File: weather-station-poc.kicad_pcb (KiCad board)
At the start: 4 copper layers, 155 x 88 mm, 136 parts, among them IC1 632723100011, IC2 TCPP01-M12, IC3 USBLC6-2SC6, IC4 BME690, IC5 S2-LPQTR, IC6 BALF-SPI2-01D3, IC7 STSAFA110S8OCD03, J1 Conn_ARM_JTAG_SWD_10, J2 61300311121, J3 61300311121, J4 61300511121, J5 61300311121, J6 687140149022, J7 687110149022, Q1 STL11N3LLH6, U1 STM32U5G9ZJTxQ, U2 BME280, U3 BMP581, Y1 NX2016SA-16MHZ-EXS00A-CS07826, Y2 NX2012SA-32.768K-STD-MUB-1, Y3 NX1612SA-50M-EXS00A-CS08403

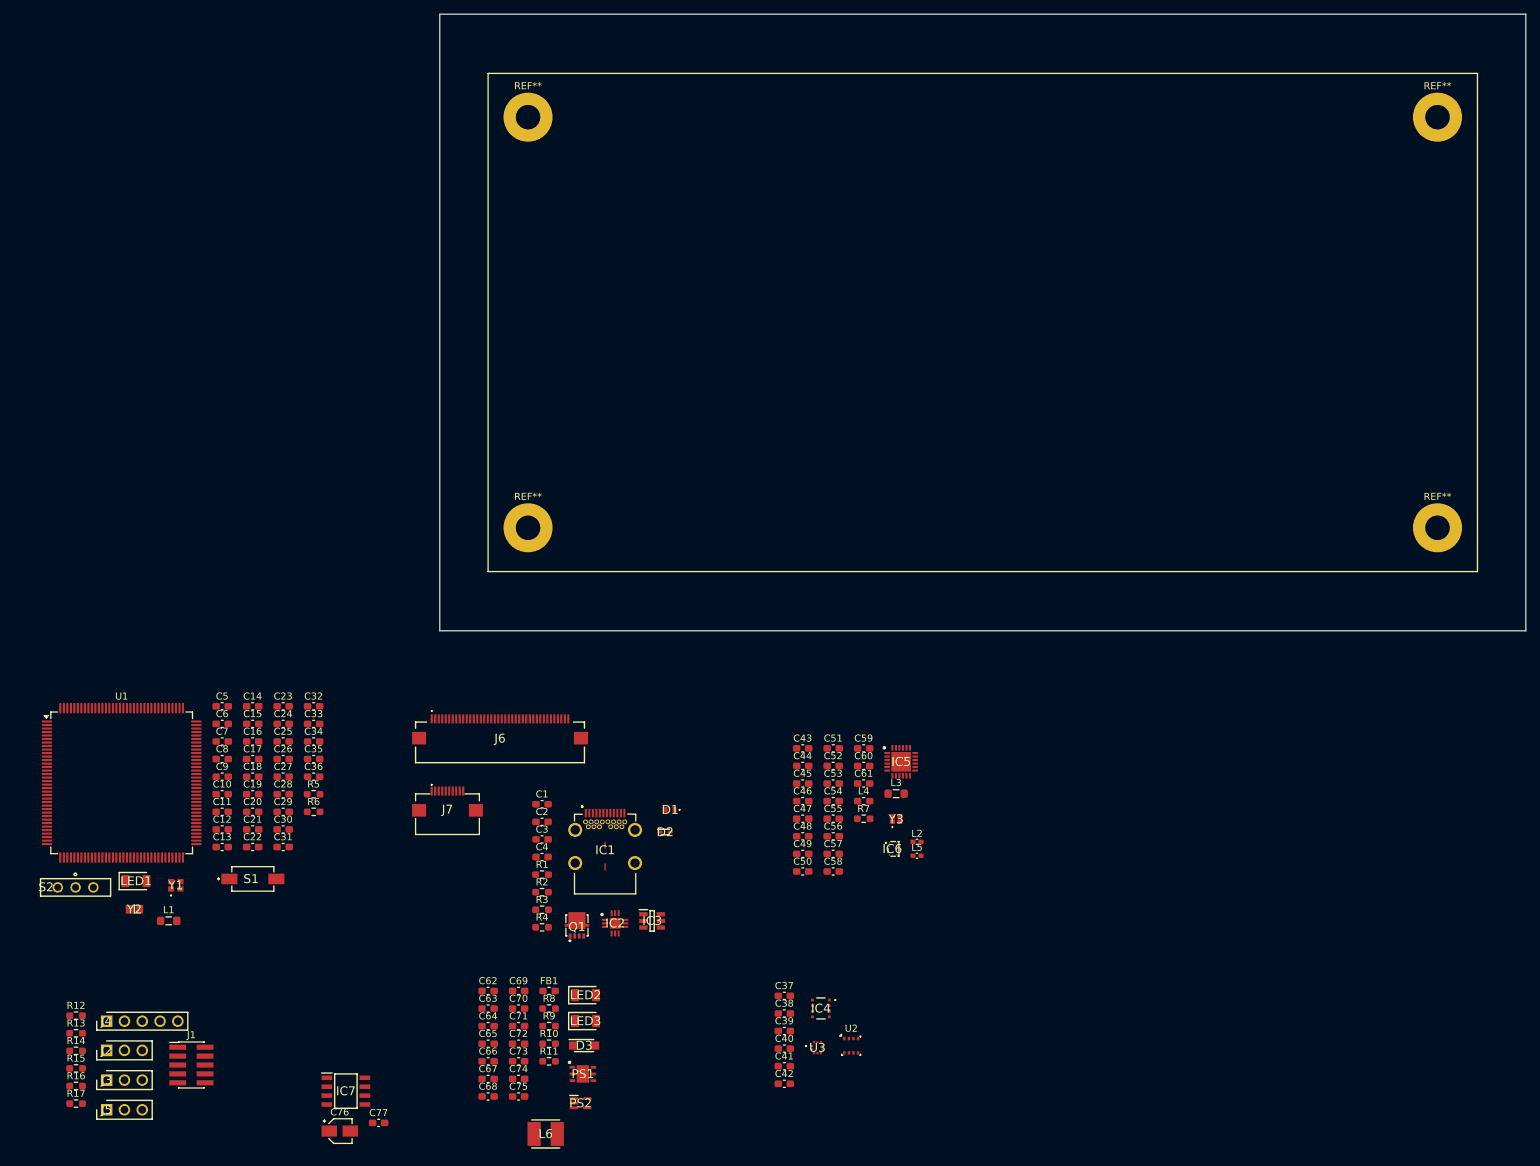
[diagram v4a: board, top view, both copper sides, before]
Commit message: LCD 10 pins connector is top and not bottom face, replace connector part
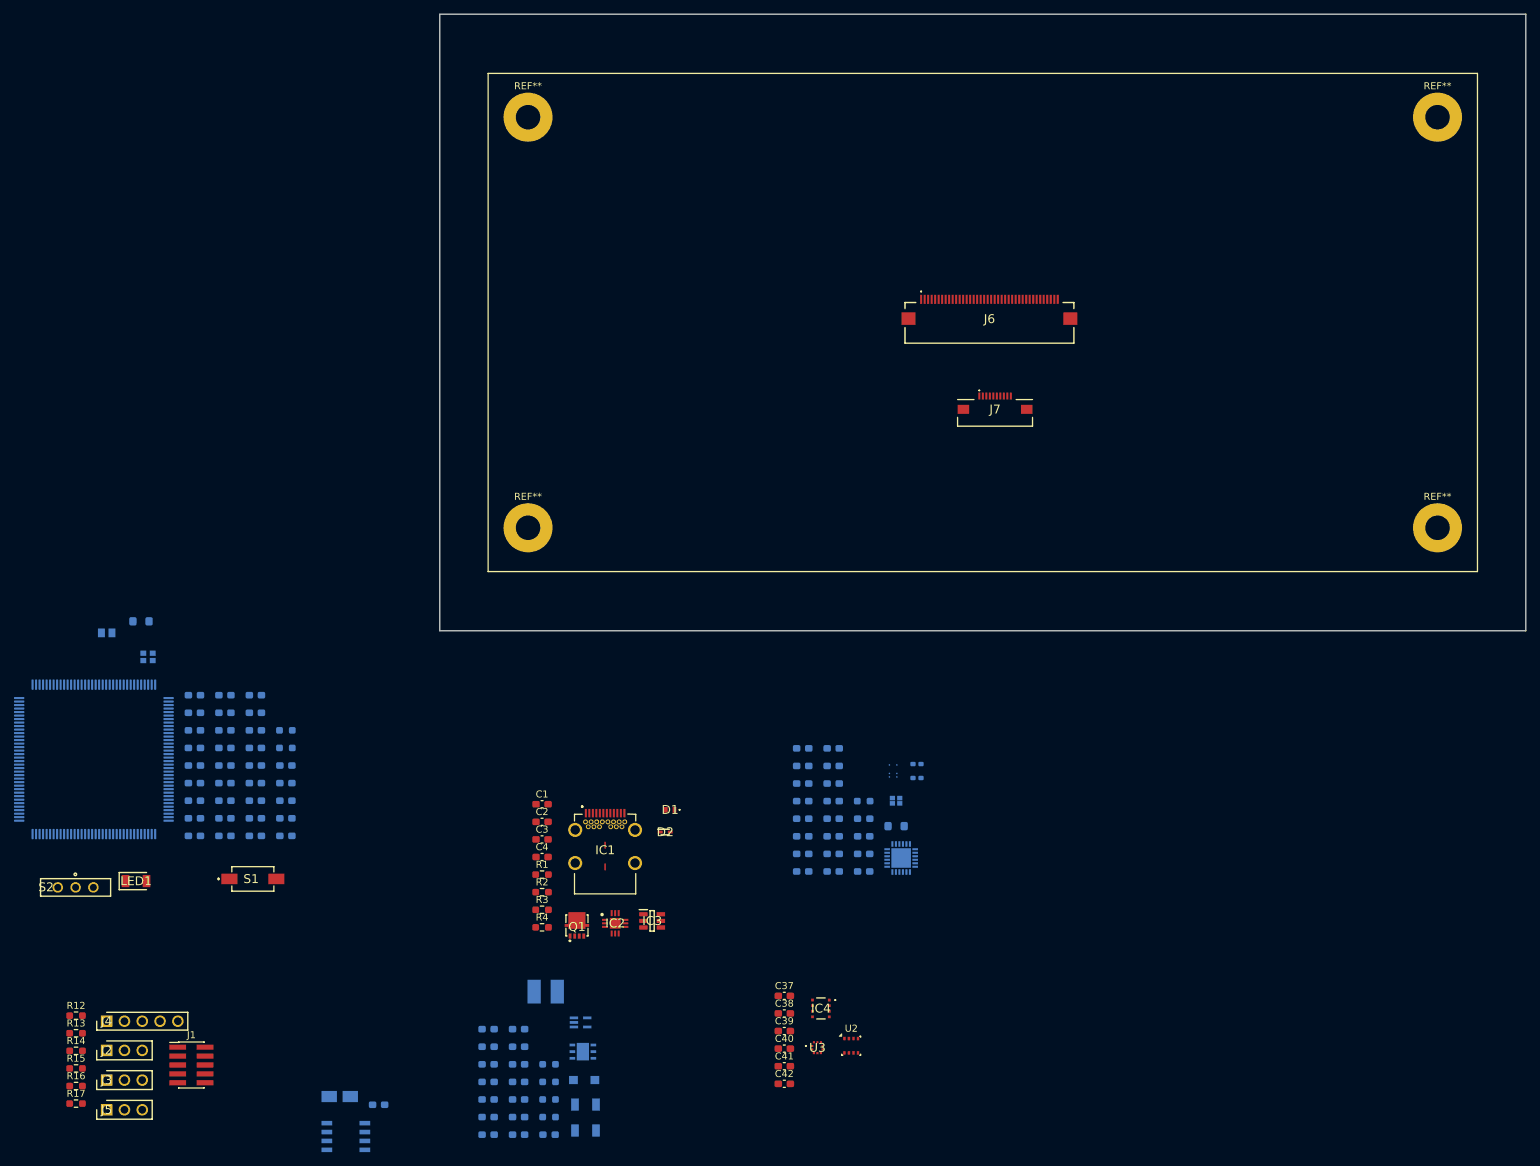
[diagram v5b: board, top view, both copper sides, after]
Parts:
- C10, C11, C12, C13, C14, C15, C16, C17, C18, C19, C20, C21, C22, C23, C24, C25, C26, C27, C28, C29, C30, C31, C32, C33, C34, C35, C36, C43, C44, C45, C46, C47, C48, C49, C5, C50, C51, C52, C53, C54, C55, C56, C57, C58, C59, C6, C60, C61, C62, C63, C64, C65, C66, C67, C68, C69, C7, C70, C71, C72, C73, C74, C75, C76, C77, C8, C9, D3, FB1, IC5, IC6, IC7, L1, L2, L3, L4, L5, L6, LED2, LED3, PS1, PS2, R10, R11, R5, R6, R7, R8, R9, U1, Y1, Y2, Y3: moved to B.Cu
- J7: value 687110149022 -> 687110183622; footprint weather-station-poc-fp:687110149022 -> weather-station-poc-fp:687110183622
- moved J7 95.5 mm to (164.7, 88.7)
- moved J6 92.0 mm to (163.8, 76.1)
- moved L1 42.9 mm to (42.8, 119.0)
- moved Y2 39.6 mm to (37.9, 120.6)
- moved Y1 32.8 mm to (43.8, 124.0)
- moved C13 22.0 mm to (50.4, 129.5)
- moved C22 22.0 mm to (54.7, 129.5)
- moved C31 22.0 mm to (59.1, 129.5)
- moved C62 20.5 mm to (92.3, 192.2)
- moved C69 20.5 mm to (96.7, 192.2)
- moved FB1 20.5 mm to (101.0, 192.2)
- moved L6 20.3 mm to (100.5, 171.8)
- moved LED2 19.3 mm to (106.2, 191.6)
- moved C14 18.9 mm to (54.7, 149.6)
- moved C32 18.9 mm to (63.4, 149.6)
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
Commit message: Place MCU and its components around
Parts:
- removed the C29 at (59.1, 134.5)
- moved S2 207.4 mm to (232.1, 89.0), turned to 180 degrees
- moved C31 144.6 mm to (177.7, 61.0), turned to -90 degrees
- moved U1 141.4 mm to (162.9, 76.3)
- moved L1 140.6 mm to (170.4, 60.2), turned to 180 degrees
- moved C9 140.4 mm to (168.1, 62.9), turned to 90 degrees
- moved C23 138.6 mm to (176.3, 75.6)
- moved C8 138.2 mm to (176.3, 85.0)
- moved C10 137.4 mm to (166.1, 62.9), turned to 90 degrees
- moved C28 137.1 mm to (173.2, 61.0), turned to -90 degrees
- moved C24 135.7 mm to (176.3, 78.6)
- moved C29 135.7 mm to (174.7, 61.0), turned to -90 degrees
- moved C30 135.7 mm to (176.2, 61.0), turned to -90 degrees
- moved C21 134.5 mm to (170.2, 62.9), turned to 90 degrees
- moved C22 134.2 mm to (176.3, 72.6)
- moved C20 129.9 mm to (163.2, 62.9), turned to 90 degrees
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- renumbered C30 to C29, C31 to C30, C32 to C31, C33 to C32, C34 to C33, C35 to C34, C36 to C35, C37 to C36, C38 to C37, C39 to C38, C40 to C39, C41 to C40, C42 to C41, C43 to C42, C44 to C43, C45 to C44, C46 to C45, C47 to C46, C48 to C47, C49 to C48, C50 to C49, C51 to C50, C52 to C51, C53 to C52, C54 to C53, C55 to C54, C56 to C55, C57 to C56, C58 to C57, C59 to C58, C60 to C59, C61 to C60, C62 to C61, C63 to C62, C64 to C63, C65 to C64, C66 to C65, C67 to C66, C68 to C67, C69 to C68, C70 to C69, C71 to C70, C72 to C71, C73 to C72, C74 to C73, C75 to C74, C76 to C75, C77 to C76
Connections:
- C28 pad 1: +3V3_CONT -> /MCU/VDD11

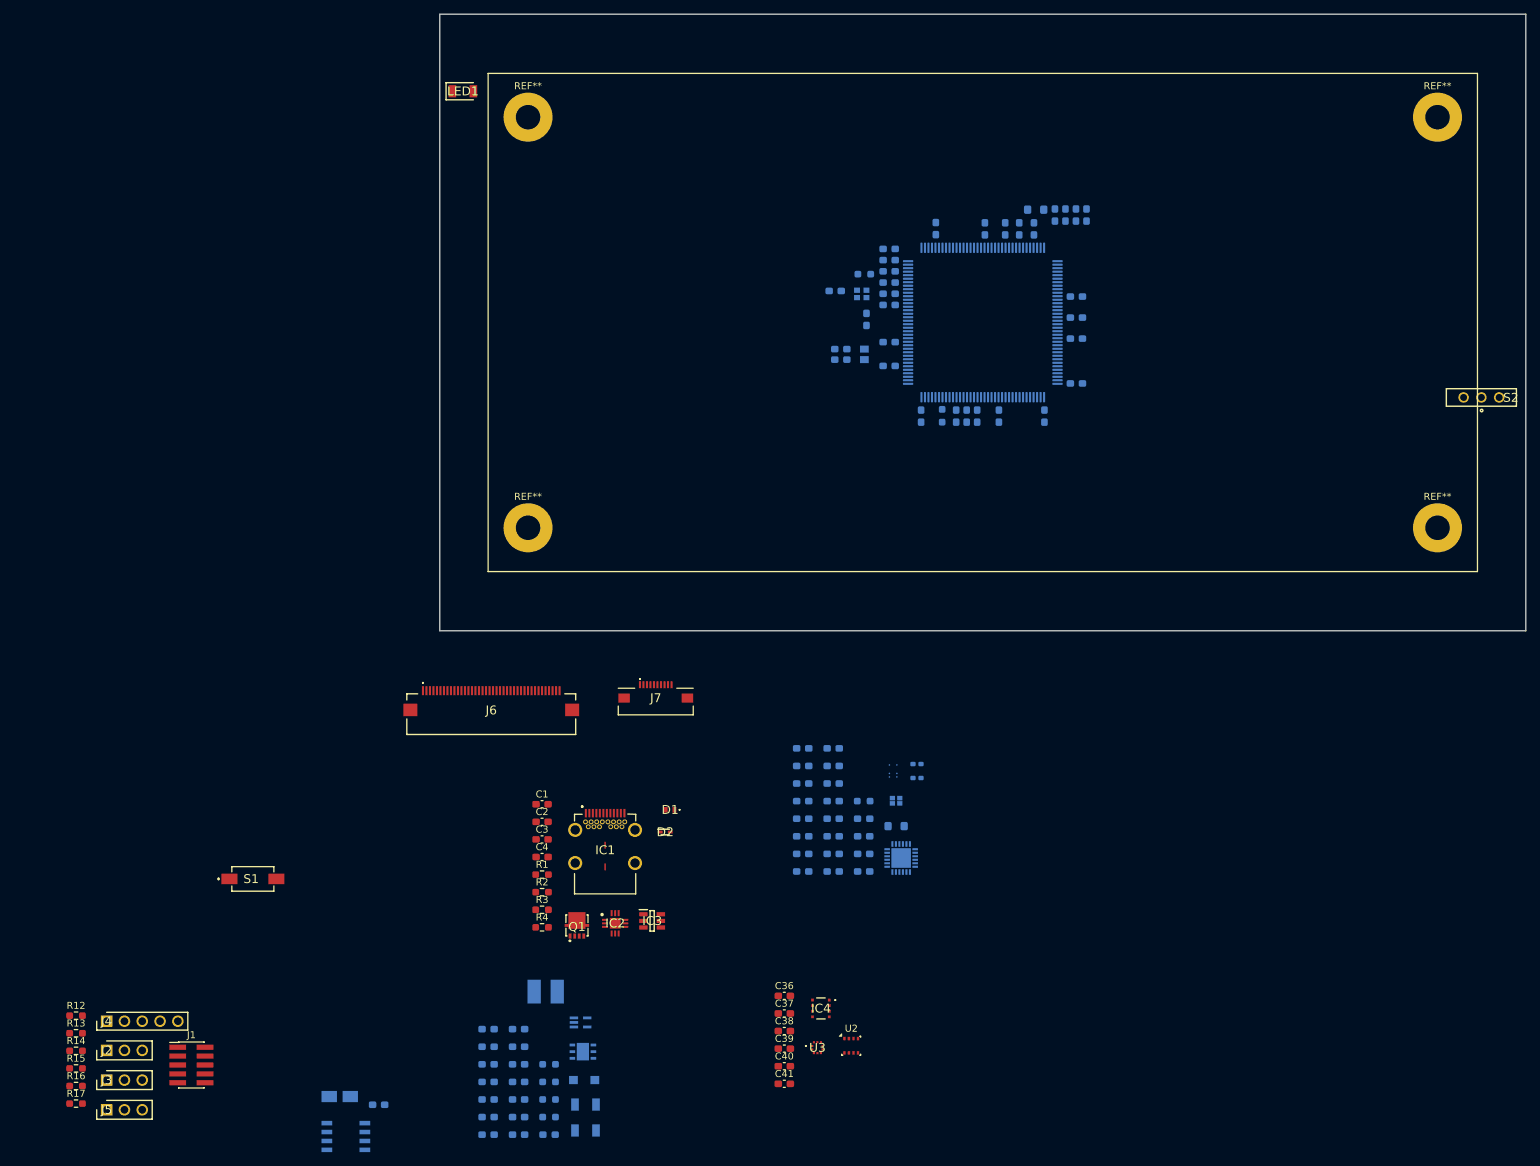
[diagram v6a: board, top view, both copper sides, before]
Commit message: Place power supplies components and STSAFE
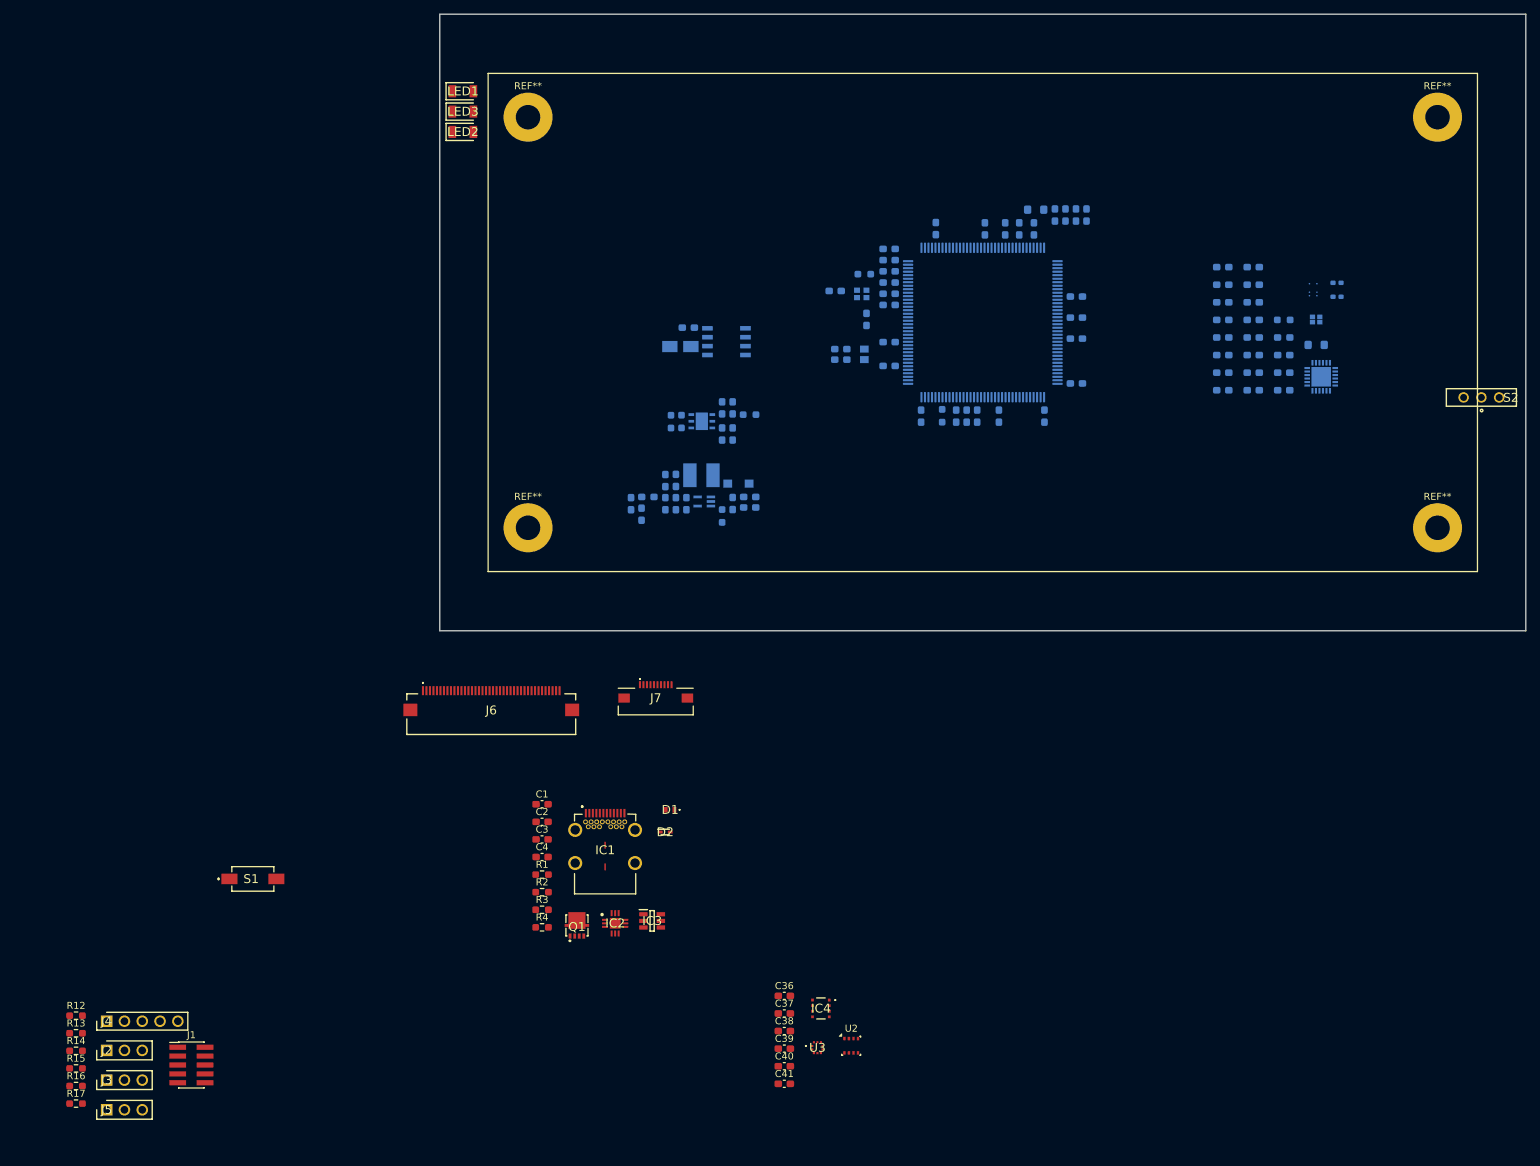
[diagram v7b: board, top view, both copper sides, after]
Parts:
- LED2, LED3: moved to F.Cu
- moved LED2 143.6 mm to (88.7, 49.1)
- moved LED3 142.8 mm to (88.7, 46.2)
- moved IC7 125.8 mm to (126.3, 79.0)
- moved C76 119.4 mm to (120.9, 77.0), turned to 180 degrees
- moved C75 117.6 mm to (119.7, 79.7), turned to 180 degrees
- moved C61 105.9 mm to (127.2, 92.2), turned to -90 degrees
- moved C63 104.2 mm to (125.7, 88.5), turned to 90 degrees
- moved C62 103.1 mm to (125.7, 92.2), turned to -90 degrees
- moved C64 102.3 mm to (127.2, 88.5), turned to 90 degrees
- moved R9 101.8 mm to (129.6, 89.5)
- moved R8 101.0 mm to (119.9, 90.4), turned to -90 degrees
- moved R10 95.8 mm to (118.4, 90.5), turned to 90 degrees
- moved FB1 92.1 mm to (115.1, 101.2)
- moved PS1 91.6 mm to (122.8, 90.4)
- moved C68 91.5 mm to (112.7, 102.2), turned to -90 degrees
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
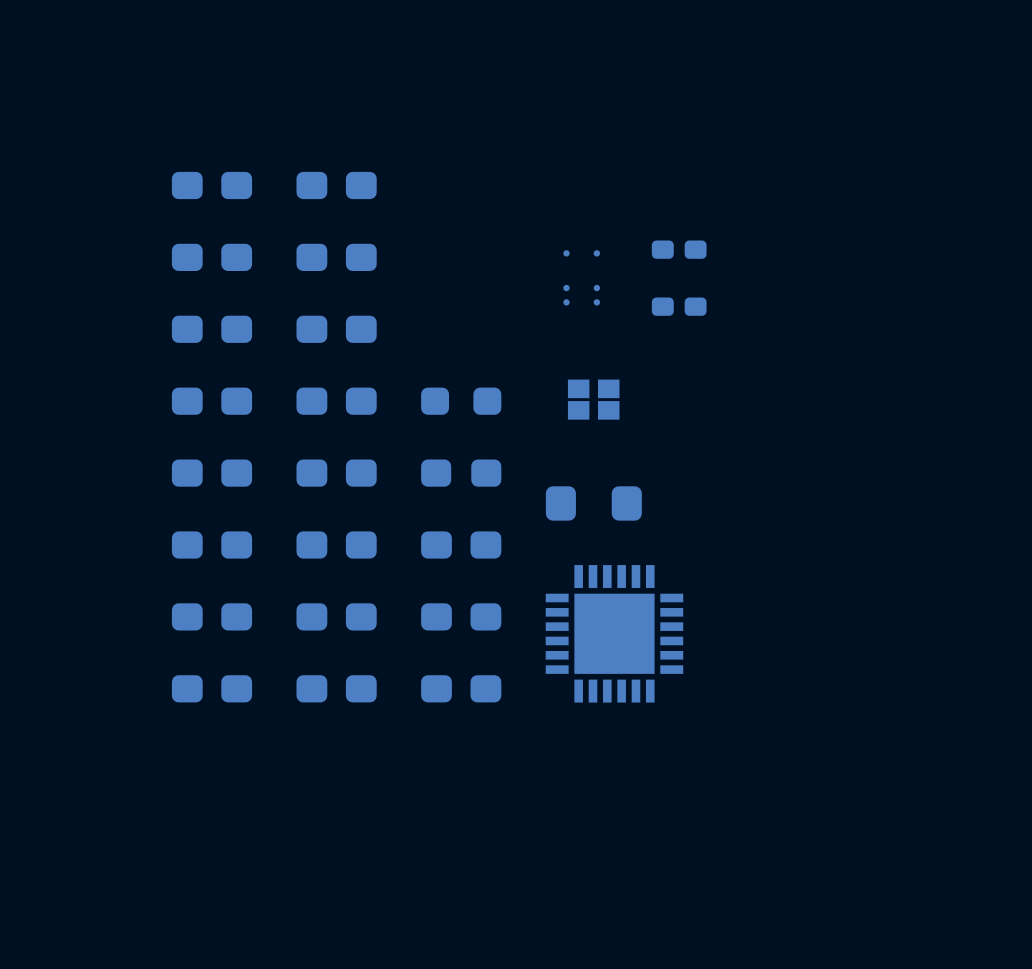
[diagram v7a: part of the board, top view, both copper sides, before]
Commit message: Place S2LP radio module on PCB
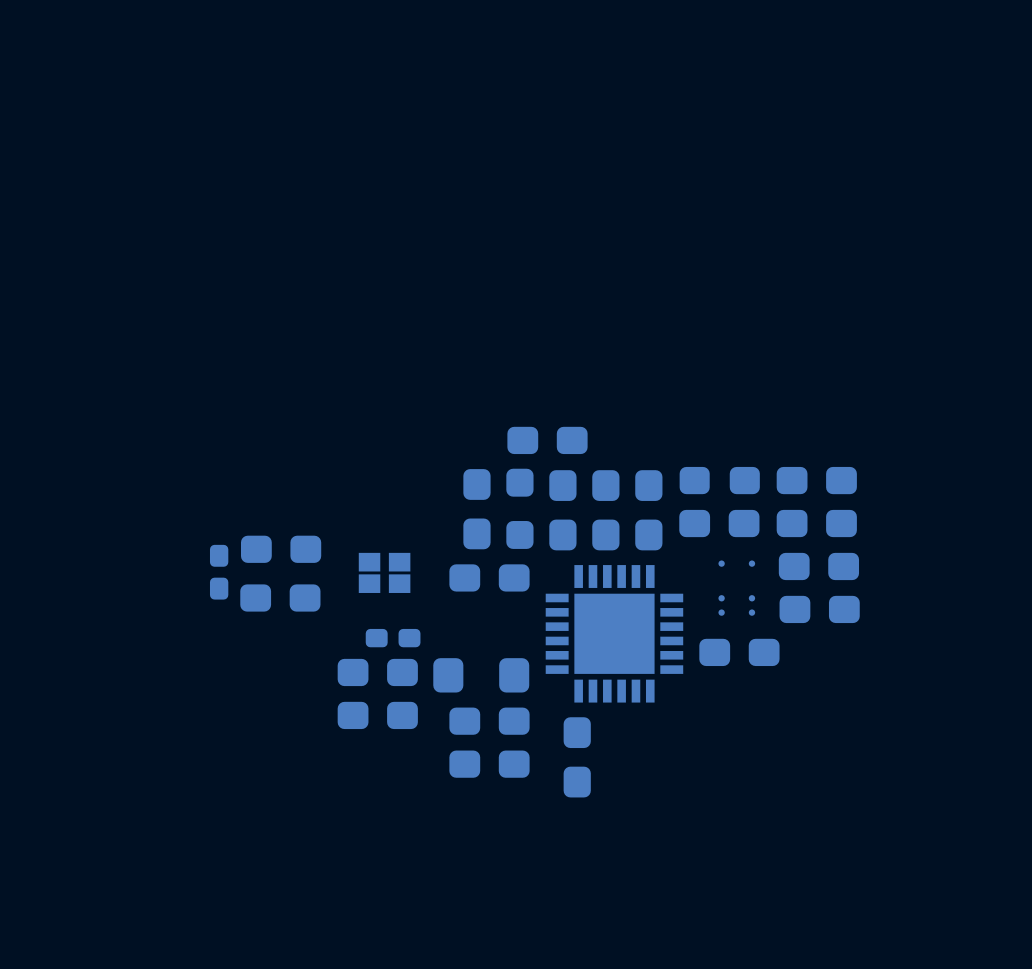
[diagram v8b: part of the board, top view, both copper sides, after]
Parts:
- moved C49 25.0 mm to (218.3, 81.7), turned to 180 degrees
- moved C48 24.5 mm to (218.4, 83.2)
- moved C57 19.7 mm to (218.3, 78.7)
- moved L5 19.6 mm to (197.4, 81.9), turned to 90 degrees
- moved C44 18.8 mm to (215.6, 84.7)
- moved C56 16.3 mm to (214.9, 80.2)
- moved L2 15.3 mm to (203.5, 84.2)
- moved C47 15.1 mm to (210.9, 79.7), turned to 90 degrees
- moved C42 14.6 mm to (208.9, 77.3)
- moved C54 13.7 mm to (206.8, 88.6), turned to 180 degrees
- moved C58 13.7 mm to (218.3, 80.2), turned to 180 degrees
- moved C43 13.7 mm to (209.9, 88.4), turned to -90 degrees
- moved IC6 12.1 mm to (215.5, 83.3)
- moved C46 11.1 mm to (202.9, 85.4), turned to 180 degrees
- moved C52 11.0 mm to (212.4, 79.7), turned to 90 degrees
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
